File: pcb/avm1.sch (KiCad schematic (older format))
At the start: 77 parts, among them J1 Video_Output, J10 Front_Conn_1, J11 Front_Conn_3, J12 Back_Conn_2, J13 Back_Conn_3, J14 Back_Conn_1, J15 Front_Conn_4, J16 Back_Conn_4, J17 VIN, J2 Jack_X_CV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

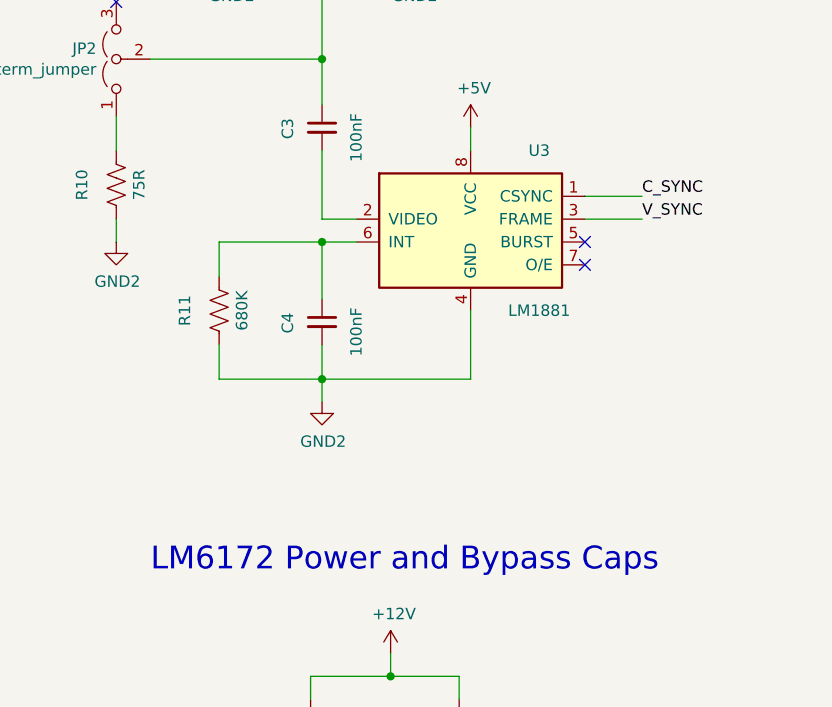
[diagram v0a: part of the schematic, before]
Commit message: Added SMD LM1881 footprint, moved a few things around
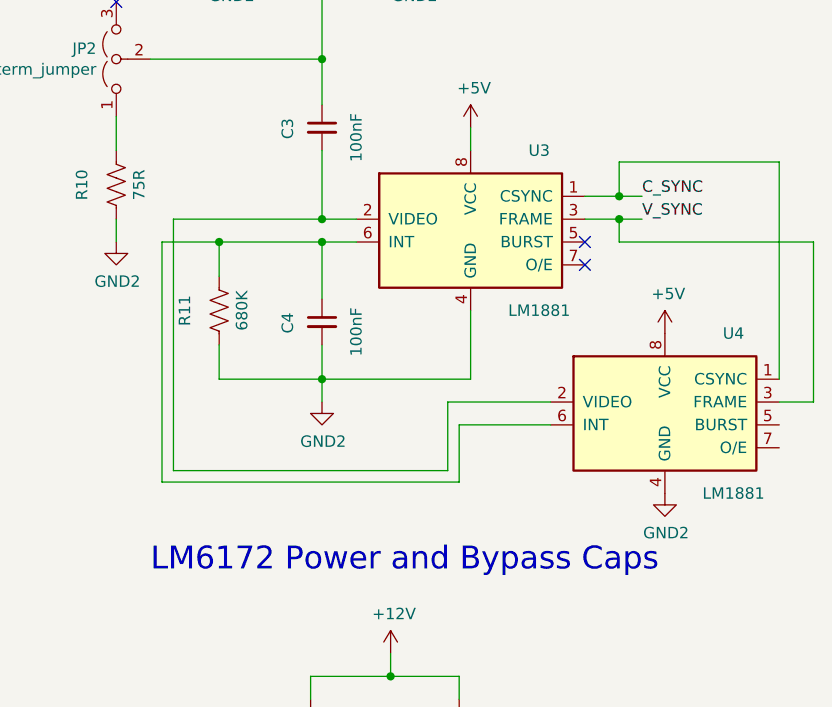
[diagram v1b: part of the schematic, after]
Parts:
- added U4: LM1881, Package_SO:SOIC-8_3.9x4.9mm_P1.27mm, symbol Video:LM1881
- R10, R20, R21, R7: footprint Resistor_THT:R_Axial_DIN0207_L6.3mm_D2.5mm_P2.54mm_Vertical -> jwm_kicad_footprints_misc:R_Axial_P7.62mm_Horizontal_LZX
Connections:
- net +5V: now also U4.8 (VCC)
- net C_SYNC: now also U4.1 (CSYNC)
- net GND2: now also U4.4 (GND)
- net V_SYNC: now also U4.3 (FRAME)
- net at C3.2, U3.2 (VIDEO): now also U4.2 (VIDEO)
- net at C4.1, R11.2, U3.6 (INT): now also U4.6 (INT)
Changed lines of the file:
@@
 F 0 "R20" V 1950 4850 50  0000 C CNN
 F 1 "100K" V 2200 4850 50  0000 C CNN
-F 2 "Resistor_THT:R_Axial_DIN0207_L6.3mm_D2.5mm_P2.54mm_Vertical" V 2140 4840 50  0001 C CNN
+F 2 "jwm_kicad_footprints_misc:R_Axial_P7.62mm_Horizontal_LZX" V 2140 4840 50  0001 C CNN
 F 3 "~" H 2100 4850 50  0001 C CNN
 	1    2100 4850
@@
 F 0 "R21" V 2800 4850 50  0000 C CNN
 F 1 "100K" V 3000 4850 50  0000 C CNN
-F 2 "Resistor_THT:R_Axial_DIN0207_L6.3mm_D2.5mm_P2.54mm_Vertical" V 2940 4840 50  0001 C CNN
+F 2 "jwm_kicad_footprints_misc:R_Axial_P7.62mm_Horizontal_LZX" V 2940 4840 50  0001 C CNN
 F 3 "~" H 2900 4850 50  0001 C CNN
 	1    2900 4850
@@
 C_SYNC
 Wire Wire Line
-	15800 3650 16050 3650
-Wire Wire Line
-	15800 3750 16050 3750
+	15800 3650 15950 3650
+Wire Wire Line
+	15800 3750 15950 3750
 Text Label 16050 3650 0    50   ~ 0
 C_SYNC
@@
 F 0 "R10" V 13900 3600 50  0000 C CNN
 F 1 "75R" V 13650 3600 50  0000 C CNN
-F 2 "Resistor_THT:R_Axial_DIN0207_L6.3mm_D2.5mm_P2.54mm_Vertical" V 13790 3590 50  0001 C CNN
+F 2 "jwm_kicad_footprints_misc:R_Axial_P7.62mm_Horizontal_LZX" V 13790 3590 50  0001 C CNN
 F 3 "~" H 13750 3600 50  0001 C CNN
 	1    13750 3600
@@
 F 0 "R7" V 9250 1200 50  0000 C CNN
 F 1 "100K" V 9450 1200 50  0000 C CNN
-F 2 "Resistor_THT:R_Axial_DIN0207_L6.3mm_D2.5mm_P2.54mm_Vertical" V 9390 1190 50  0001 C CNN
+F 2 "jwm_kicad_footprints_misc:R_Axial_P7.62mm_Horizontal_LZX" V 9390 1190 50  0001 C CNN
 F 3 "~" H 9350 1200 50  0001 C CNN
 	1    9350 1200
@@
 Wire Notes Line
 	4700 1150 4700 550
+$Comp
+L Video:LM1881 U4
+U 1 1 61961780
+P 16150 4650
+F 0 "U4" H 16450 5050 50  0000 C CNN
+F 1 "LM1881" H 16450 4350 50  0000 C CNN
+F 2 "Package_SO:SOIC-8_3.9x4.9mm_P1.27mm" H 16150 4650 50  0001 C CNN
+F 3 "" H 16150 4650 50  0001 C CNN
+	1    16150 4650
+	1    0    0    -1
+$EndComp
+Wire Wire Line
+	16650 4450 16650 3500
+Wire Wire Line
+	16650 3500 15950 3500
+Wire Wire Line
+	15950 3500 15950 3650
+Connection ~ 15950 3650
+Wire Wire Line
+	15950 3650 16050 3650
+Wire Wire Line
+	16650 4550 16800 4550
+Wire Wire Line
+	16800 4550 16800 3850
+Wire Wire Line
+	16800 3850 15950 3850
+Wire Wire Line
+	15950 3850 15950 3750
+Connection ~ 15950 3750
+Wire Wire Line
+	15950 3750 16050 3750
+Wire Wire Line
+	15650 4550 15200 4550
+Wire Wire Line
+	15200 4550 15200 4850
+Wire Wire Line
+	15200 4850 14000 4850
+Wire Wire Line
+	14000 4850 14000 3750
+Wire Wire Line
+	14000 3750 14650 3750
+Connection ~ 14650 3750
+Wire Wire Line
+	15650 4650 15250 4650
+Wire Wire Line
+	15250 4650 15250 4900
+Wire Wire Line
+	15250 4900 13950 4900
+Wire Wire Line
+	13950 4900 13950 3850
+Wire Wire Line
+	13950 3850 14200 3850
+Connection ~ 14200 3850
+$Comp
+L power:GND2 #PWR02
+U 1 1 619CBB71
+P 16150 4950
+F 0 "#PWR02" H 16150 4700 50  0001 C CNN
+F 1 "GND2" H 16155 4777 50  0000 C CNN
+F 2 "" H 16150 4950 50  0001 C CNN
+F 3 "" H 16150 4950 50  0001 C CNN
+	1    16150 4950
+	1    0    0    -1
+$EndComp
+$Comp
+L power:+5V #PWR01
+U 1 1 619CC292
+P 16150 4250
+F 0 "#PWR01" H 16150 4100 50  0001 C CNN
+F 1 "+5V" H 16165 4423 50  0000 C CNN
+F 2 "" H 16150 4250 50  0001 C CNN
+F 3 "" H 16150 4250 50  0001 C CNN
+	1    16150 4250
+	1    0    0    -1
+$EndComp
 $EndSCHEMATC
